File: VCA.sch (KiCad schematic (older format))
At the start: 29 parts, among them Q401 2N3904, Q402 2N3906, Q403 2N3904, U402 LM13700, U605 TL074

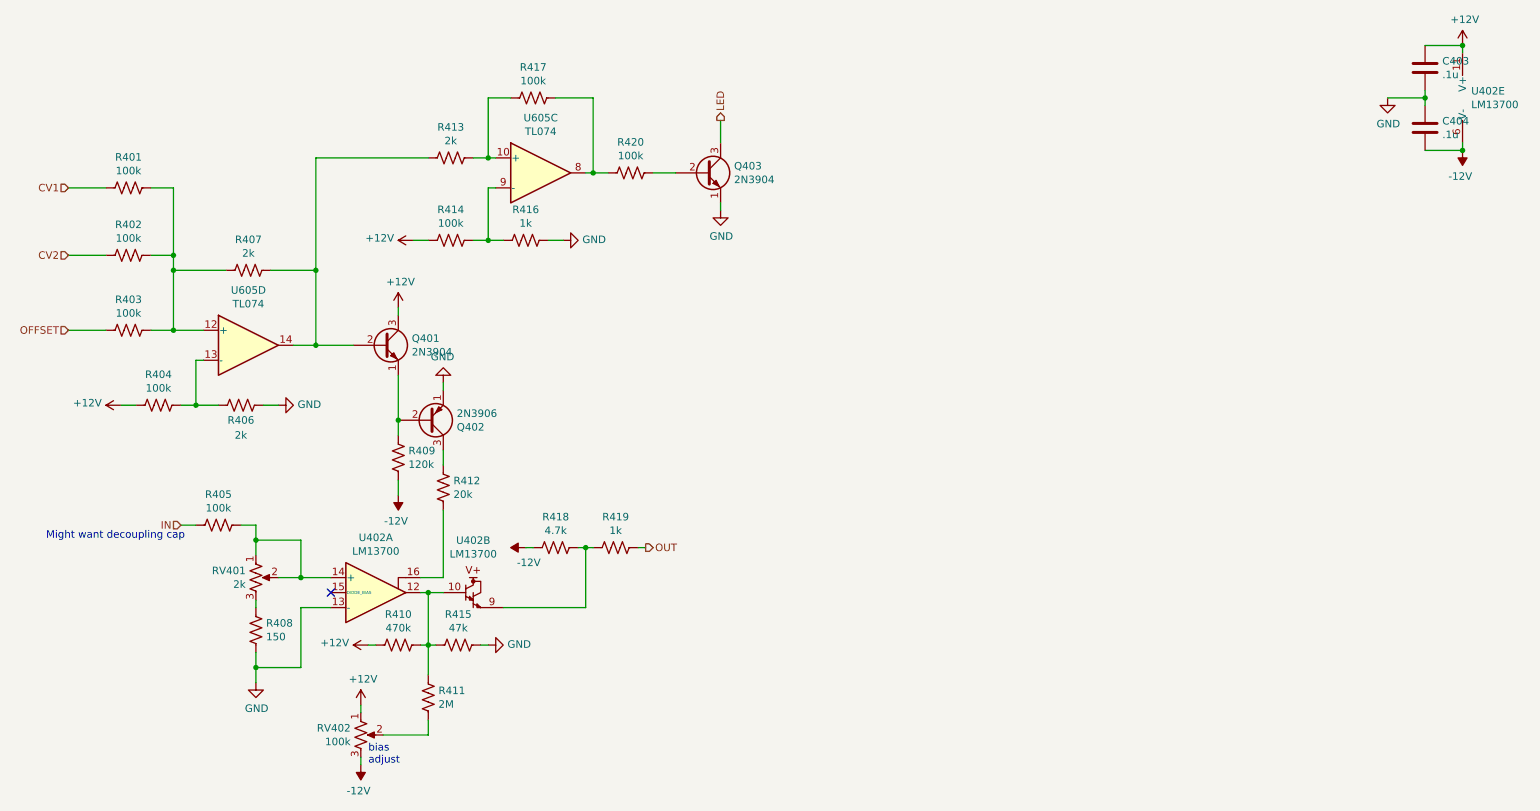
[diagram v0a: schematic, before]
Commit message: deleted extra lm13700
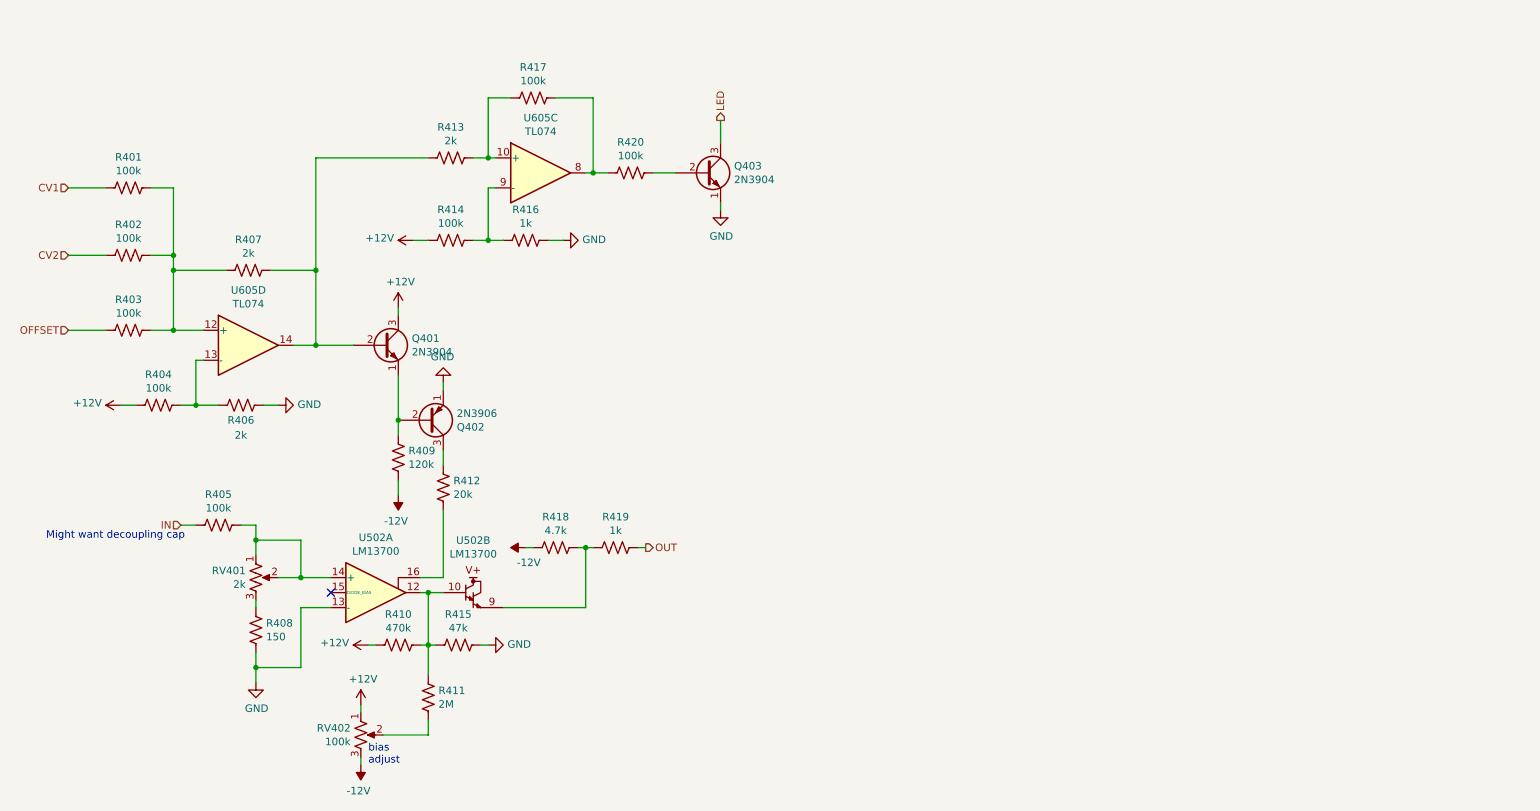
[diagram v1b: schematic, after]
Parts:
- removed C403, C404: .1u, Capacitor_THT:C_Disc_D4.7mm_W2.5mm_P5.00mm, symbol Device:C
- removed unit 5 of U402
- renumbered U402 to U502
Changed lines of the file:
@@
 $EndComp
 $Comp
-L Amplifier_Operational:LM13700 U402
+L Amplifier_Operational:LM13700 U502
 U 1 1 603B900F
 P 3250 4650
-F 0 "U402" H 3250 4283 50  0000 C CNN
+F 0 "U502" H 3250 4283 50  0000 C CNN
 F 1 "LM13700" H 3250 4374 50  0000 C CNN
 F 2 "Package_DIP:DIP-16_W7.62mm" H 2950 4675 50  0001 C CNN
@@
 $EndComp
 $Comp
-L Amplifier_Operational:LM13700 U402
+L Amplifier_Operational:LM13700 U502
 U 2 1 603BBB89
 P 4000 4650
-F 0 "U402" H 3900 4998 50  0000 C CNN
+F 0 "U502" H 3900 4998 50  0000 C CNN
 F 1 "LM13700" H 3900 4907 50  0000 C CNN
 F 2 "Package_DIP:DIP-16_W7.62mm" H 3700 4675 50  0001 C CNN
@@
 	1    0    0    -1
 $EndComp
-$Comp
-L Amplifier_Operational:LM13700 U402
-U 5 1 603BCA2E
-P 10600 1350
-F 0 "U402" H 10558 1396 50  0000 L CNN
-F 1 "LM13700" H 10558 1305 50  0000 L CNN
-F 2 "Package_DIP:DIP-16_W7.62mm" H 10300 1375 50  0001 C CNN
-F 3 "http://www.ti.com/lit/ds/symlink/lm13700.pdf" H 10300 1375 50  0001 C CNN
-	5    10600 1350
-	1    0    0    -1
-$EndComp
-Wire Wire Line
-	10500 1050 10500 1000
-Wire Wire Line
-	10500 1700 10500 1650
-$Comp
-L power:-12V #PWR0419
-U 1 1 603C5D74
-P 10500 1700
-F 0 "#PWR0419" H 10500 1800 50  0001 C CNN
-F 1 "-12V" H 10515 1873 50  0000 C CNN
-F 2 "" H 10500 1700 50  0001 C CNN
-F 3 "" H 10500 1700 50  0001 C CNN
-	1    10500 1700
-	-1   0    0    1
-$EndComp
-$Comp
-L power:+12V #PWR0418
-U 1 1 603C6B83
-P 10500 1000
-F 0 "#PWR0418" H 10500 850 50  0001 C CNN
-F 1 "+12V" H 10515 1173 50  0000 C CNN
-F 2 "" H 10500 1000 50  0001 C CNN
-F 3 "" H 10500 1000 50  0001 C CNN
-	1    10500 1000
-	1    0    0    -1
-$EndComp
-$Comp
-L power:GND #PWR0415
-U 1 1 603C7C2A
-P 10000 1350
-F 0 "#PWR0415" H 10000 1100 50  0001 C CNN
-F 1 "GND" H 10005 1177 50  0000 C CNN
-F 2 "" H 10000 1350 50  0001 C CNN
-F 3 "" H 10000 1350 50  0001 C CNN
-	1    10000 1350
-	1    0    0    -1
-$EndComp
-$Comp
-L Device:C C403
-U 1 1 603C9F79
-P 10250 1150
-F 0 "C403" H 10365 1196 50  0000 L CNN
-F 1 ".1u" H 10365 1105 50  0000 L CNN
-F 2 "Capacitor_THT:C_Disc_D4.7mm_W2.5mm_P5.00mm" H 10288 1000 50  0001 C CNN
-F 3 "~" H 10250 1150 50  0001 C CNN
-	1    10250 1150
-	1    0    0    -1
-$EndComp
-$Comp
-L Device:C C404
-U 1 1 603CFBBF
-P 10250 1550
-F 0 "C404" H 10365 1596 50  0000 L CNN
-F 1 ".1u" H 10365 1505 50  0000 L CNN
-F 2 "Capacitor_THT:C_Disc_D4.7mm_W2.5mm_P5.00mm" H 10288 1400 50  0001 C CNN
-F 3 "~" H 10250 1550 50  0001 C CNN
-	1    10250 1550
-	1    0    0    -1
-$EndComp
-Wire Wire Line
-	10250 1700 10500 1700
-Connection ~ 10500 1700
-Wire Wire Line
-	10250 1000 10500 1000
-Connection ~ 10500 1000
 Wire Wire Line
 	3700 4100 3700 4550
@@
 Text HLabel 5550 1500 1    50   Output ~ 0
 LED
-Wire Wire Line
-	10250 1300 10250 1350
-Wire Wire Line
-	10250 1350 10000 1350
-Connection ~ 10250 1350
-Wire Wire Line
-	10250 1350 10250 1400
 Text Notes 3200 5800 0    50   ~ 0
 bias\nadjust

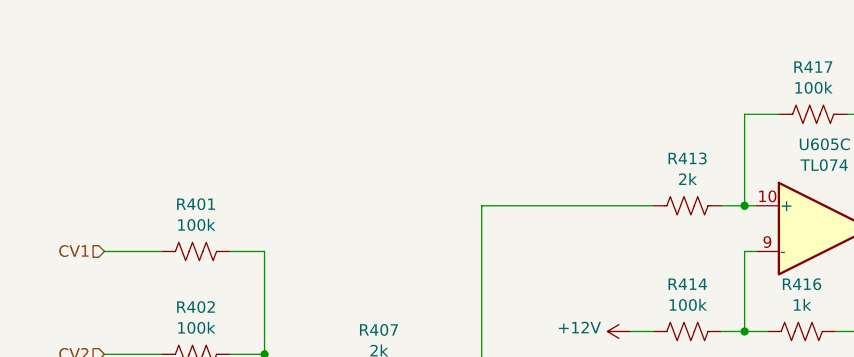
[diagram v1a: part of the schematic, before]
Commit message: Documenting op amp issue
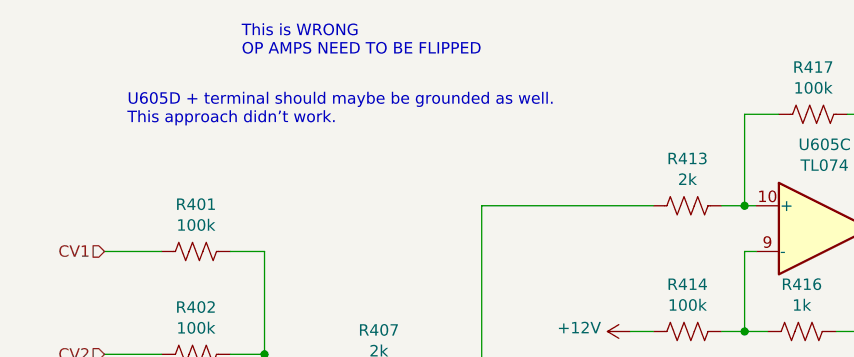
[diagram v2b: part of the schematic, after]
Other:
- note added: "This is WRONG\nOP AMPS NEED TO BE FLIPPED"
- note added: "U605D + terminal should maybe be grounded as well. \nThis approach didn’t work."
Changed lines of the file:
@@
 Text Notes 3200 5800 0    50   ~ 0
 bias\nadjust
+Text Notes 1800 1100 0    50   ~ 0
+This is WRONG\nOP AMPS NEED TO BE FLIPPED
+Text Notes 1300 1400 0    50   ~ 0
+U605D + terminal should maybe be grounded as well. \nThis approach didn’t work.
 $EndSCHEMATC
